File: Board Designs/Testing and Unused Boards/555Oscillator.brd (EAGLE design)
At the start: 44.1 x 30.5 mm, 8 parts

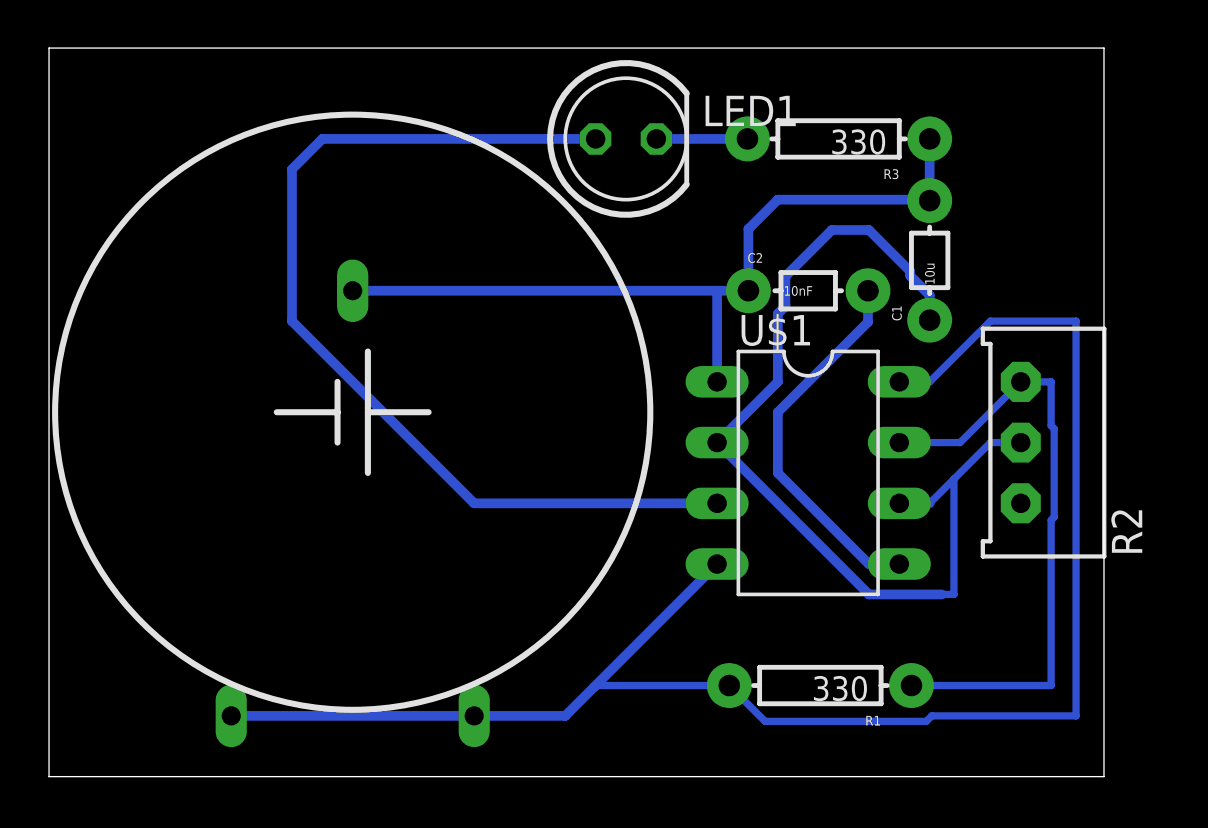
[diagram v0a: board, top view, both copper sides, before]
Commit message: Modified solder test board for jlc
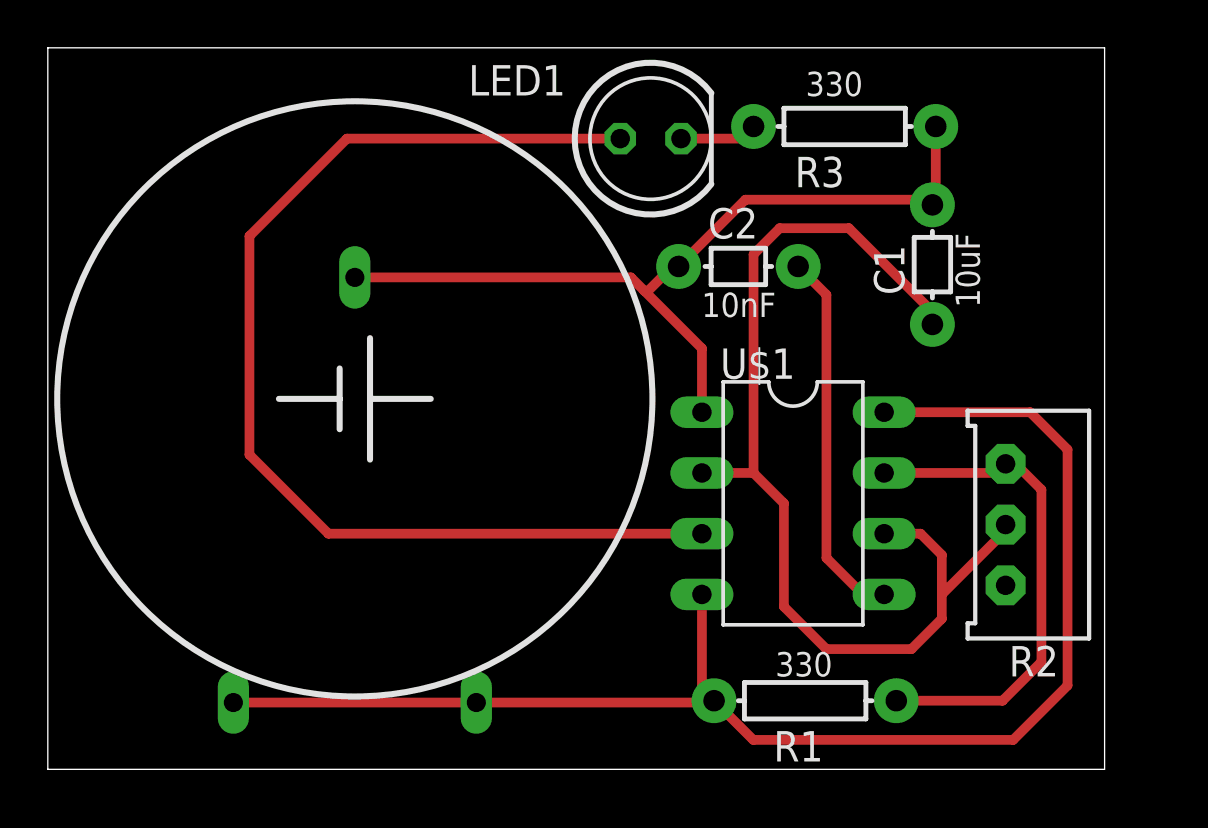
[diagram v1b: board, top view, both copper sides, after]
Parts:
- C1: value 10u -> 10uF
- moved R2 3.49 mm to (41.3, 10.5)
- moved C2 3.09 mm to (28.8, 21.3)
- moved U$1 1.42 mm to (31.1, 11.4)
- moved LED1 1.03 mm to (25.2, 26.7)
- moved R1 0.90 mm to (31.6, 3.17)
- moved R3 0.58 mm to (33.3, 27.2)
- moved U$2 0.57 mm to (12.8, 15.8)
- moved C1 0.21 mm to (36.9, 21.4)
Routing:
- net N$8: track 68.8 -> 60.5 mm
- net N$9: track 40.5 -> 46.6 mm
- net N$3: track 26.0 -> 21.3 mm
- net N$13: track 40.7 -> 44.7 mm
- net N$2: track 33.7 -> 35.5 mm
- net N$10: track 3.81 -> 3.25 mm
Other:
- board size 44.1 x 30.5 mm -> 44.2 x 30.2 mm
